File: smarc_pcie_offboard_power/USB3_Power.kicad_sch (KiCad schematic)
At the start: 16 parts, among them U501 TPS2553, U502 TPS2553

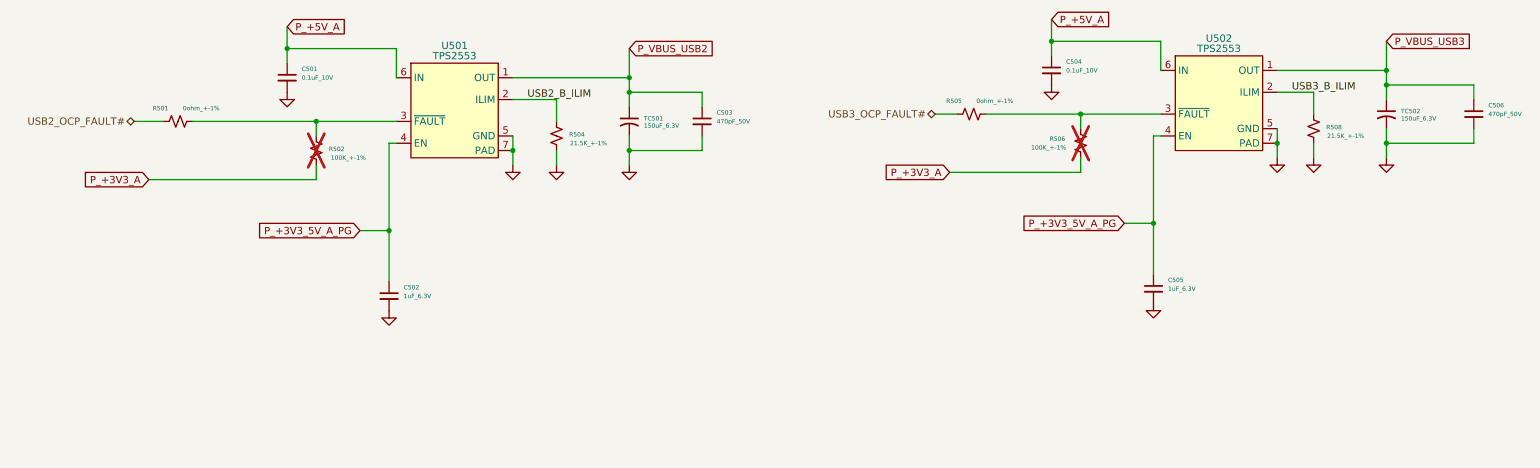
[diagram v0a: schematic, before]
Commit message: power supply validated by codex
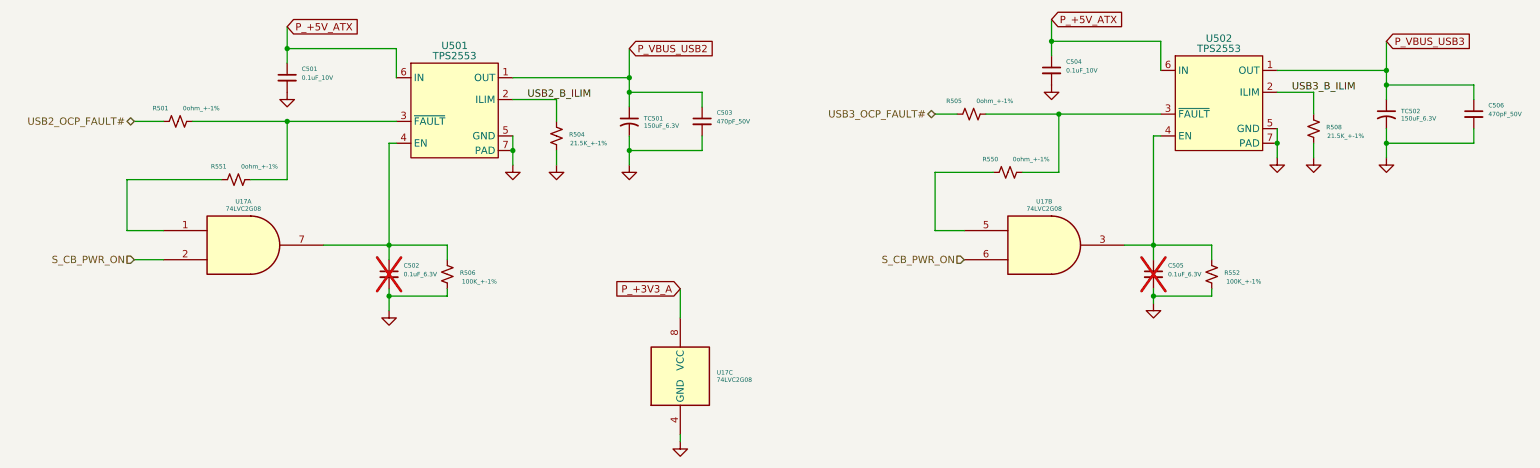
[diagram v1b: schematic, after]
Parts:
- removed R502: 100K_+-1%, symbol Device:R_Small_US
- added R550, R551: 0ohm_+-1%, symbol Device:R_Small_US
- added R552: 100K_+-1%, symbol Device:R_Small_US
- added U17: 74LVC2G08, symbol 74xGxx:74LVC2G08
- C502, C505: value 1uF_6.3V -> 0.1uF_6.3V; now not fitted
- R506: now fitted
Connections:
- net GND: now also R506.1, R552.1, U17.4 (GND)
- net P_+3V3_A: now also U17.8 (VCC); no longer R506.1
- net at R505.2, U502.3 (~{FAULT}): now also R550.2; no longer R506.2
- net at R501.2, U501.3 (~{FAULT}): now also R551.2
- net P_+3V3_5V_A_PG: no longer names the net of C505.1, U502.4 (EN)
- net P_+3V3_5V_A_PG: now also R552.2, U17.3; no longer C502.1, U501.4 (EN)
- net P_+5V_A renamed P_+5V_ATX
- new net: C502.1, R506.2, U17.7, U501.4 (EN)
- new net: R550.1, U17.5
- new net: R551.1, U17.1
- new net S_CB_PWR_ON: U17.2, U17.6
